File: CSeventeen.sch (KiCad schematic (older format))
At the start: 0 parts

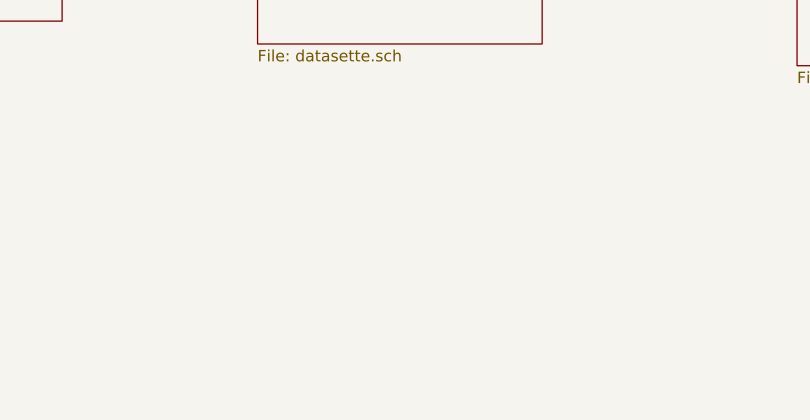
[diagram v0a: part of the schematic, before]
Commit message: Add Selection circuit
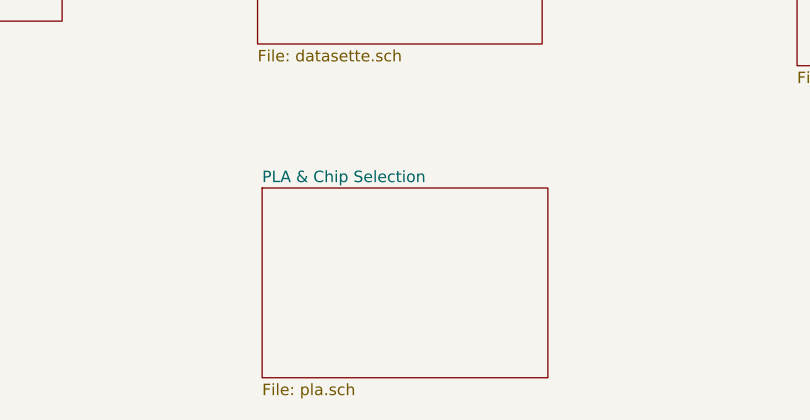
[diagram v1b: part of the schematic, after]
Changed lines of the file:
@@
 $Descr A4 11693 8268
 encoding utf-8
-Sheet 1 9
+Sheet 1 10
 Title ""
 Date ""
@@
 F1 "rom.sch" 50
 $EndSheet
+$Sheet
+S 3540 4685 1250 830
+U 5EE7AAEB
+F0 "PLA & Chip Selection" 50
+F1 "pla.sch" 50
+$EndSheet
 $EndSCHEMATC

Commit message: Add AV output and... we're done!
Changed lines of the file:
@@
 $Descr A4 11693 8268
 encoding utf-8
-Sheet 1 10
+Sheet 1 11
 Title ""
 Date ""
@@
 F1 "pla.sch" 50
 $EndSheet
+$Sheet
+S 5880 4680 1260 825
+U 5E019FCB
+F0 "Audio/Video Output" 50
+F1 "avout.sch" 50
+$EndSheet
 $EndSCHEMATC

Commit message: Fix schematics here and there
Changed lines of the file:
@@
 encoding utf-8
 Sheet 1 11
-Title ""
-Date ""
-Rev ""
-Comp ""
-Comment1 ""
-Comment2 ""
+Title "CSeventeen"
+Date "2020-01-03"
+Rev "1git"
+Comp "SukkoPera"
+Comment1 "Licensed under CC BY-NC-SA 4.0"
+Comment2 "WARNING: These schematics might contain errors!"
 Comment3 ""
 Comment4 ""
 $EndDescr
 $Sheet
-S 3320 1240 1265 745
+S 1580 1230 1300 750
+U 5E4A81E1
+F0 "CPU" 50
+F1 "cpu.sch" 50
+$EndSheet
+$Sheet
+S 3990 1240 1300 750
 U 5DE044CB
 F0 "TED" 50
@@
 $EndSheet
 $Sheet
-S 1405 3140 1260 815
+S 6400 1245 1300 750
+U 5E4A465A
+F0 "RAM" 50
+F1 "ram.sch" 50
+$EndSheet
+$Sheet
+S 8810 1260 1300 750
+U 5EE476E1
+F0 "ROMs" 50
+F1 "rom.sch" 50
+$EndSheet
+$Sheet
+S 1580 3180 1300 750
 U 5DECEF6F
 F0 "Keyboard & Joystick" 50
@@
 $EndSheet
 $Sheet
-S 5775 1245 1275 835
-U 5E4A465A
-F0 "RAM" 50
-F1 "ram.sch" 50
+S 3990 3180 1300 750
+U 5ECB474B
+F0 "Datassette & Serial Bus" 50
+F1 "datasette.sch" 50
 $EndSheet
 $Sheet
-S 1440 1230 1255 740
-U 5E4A81E1
-F0 "CPU" 50
-F1 "cpu.sch" 50
-$EndSheet
-$Sheet
-S 5880 3285 1250 865
+S 6400 3180 1300 750
 U 5E6A379E
 F0 "Expansion Port" 50
@@
 $EndSheet
 $Sheet
-S 8160 3255 1375 870
+S 8810 3180 1300 750
 U 5EACE220
 F0 "Power & Misc" 50
@@
 $EndSheet
 $Sheet
-S 3520 3135 1245 920
-U 5ECB474B
-F0 "Datassette & Serial Bus" 50
-F1 "datasette.sch" 50
-$EndSheet
-$Sheet
-S 8130 1260 1365 870
-U 5EE476E1
-F0 "ROMs" 50
-F1 "rom.sch" 50
-$EndSheet
-$Sheet
-S 3540 4685 1250 830
+S 3990 5130 1300 750
 U 5EE7AAEB
 F0 "PLA & Chip Selection" 50
@@
 $EndSheet
 $Sheet
-S 5880 4680 1260 825
+S 6400 5130 1300 750
 U 5E019FCB
 F0 "Audio/Video Output" 50
